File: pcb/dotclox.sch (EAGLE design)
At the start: 1 part, among them IC1 DS1307Z

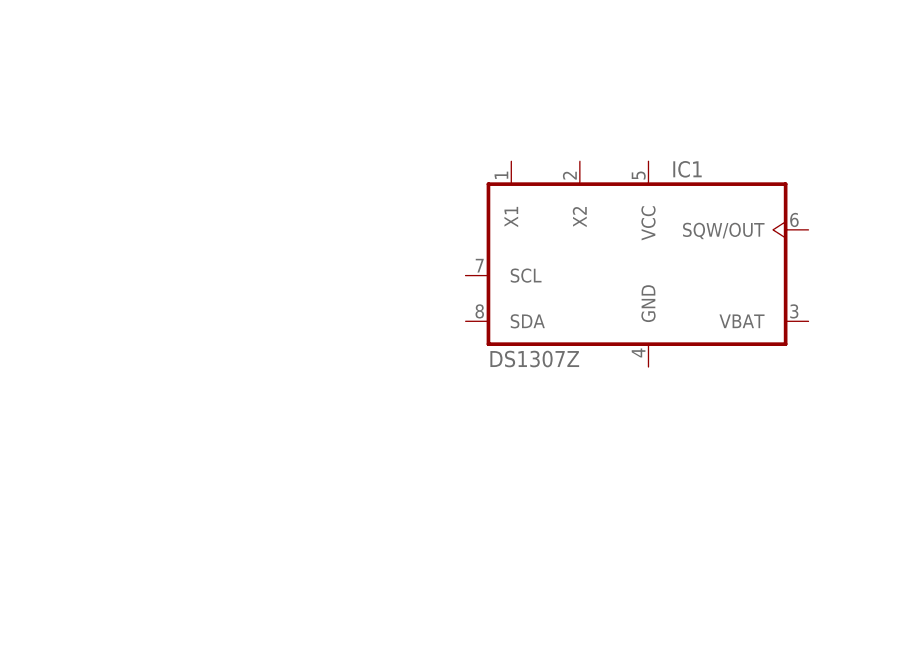
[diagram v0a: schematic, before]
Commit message: add basic parts to sch and brd
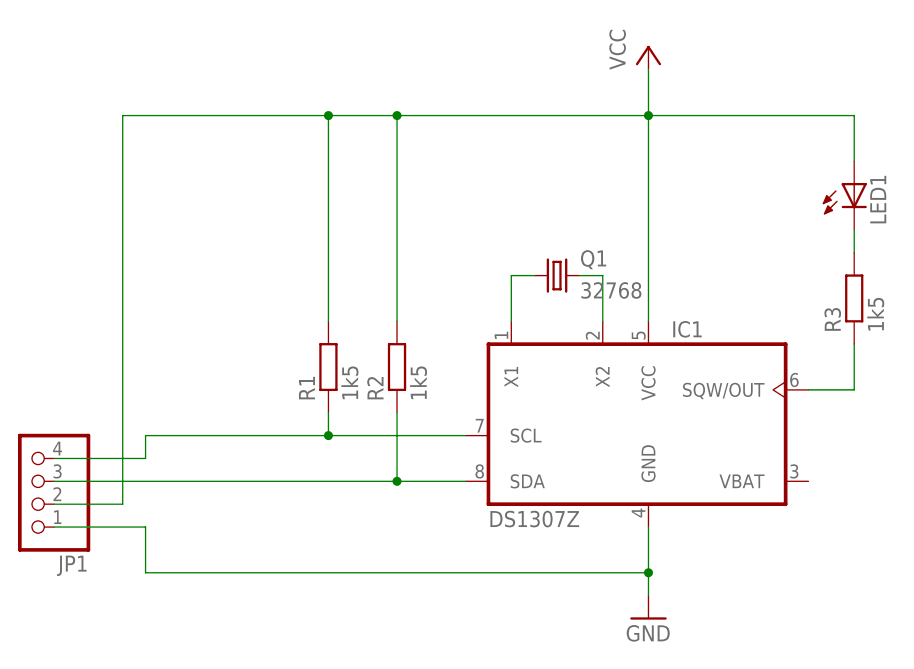
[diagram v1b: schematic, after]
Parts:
- added JP1: (no value), pinhead:PINHD-1X4
- added LED1: (no value), led:LED3MM
- added Q1: 32768, crystal:CRYSTALTC26H
- added R1, R2, R3: 1k5, rcl:R-EU_R0603
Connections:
- new net GND: IC1.GND, JP1.1
- new net N$1: IC1.X1, Q1.1
- new net N$2: IC1.X2, Q1.2
- new net N$3: IC1.SQW/OUT, R3.1
- new net N$4: LED1.C, R3.2
- new net SCL: IC1.SCL, JP1.4, R1.1
- new net SDA: IC1.SDA, JP1.3, R2.1
- new net VCC: IC1.VCC, JP1.2, LED1.A, R1.2, R2.2
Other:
- moved on the sheet: IC1
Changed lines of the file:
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@@
 <?xml version="1.0" encoding="utf-8"?>
 <!DOCTYPE eagle SYSTEM "eagle.dtd">
-<eagle version="7.2.0">
+<eagle version="7.5.0">
 <drawing>
 <settings>
@@
 <parts>
 <part name="IC1" library="n39" deviceset="DS1307" device="Z"/>
+<part name="R1" library="rcl" deviceset="R-EU_" device="R0603" value="1k5"/>
+<part name="R2" library="rcl" deviceset="R-EU_" device="R0603" value="1k5"/>
+<part name="P+1" library="supply1" deviceset="VCC" device=""/>
+<part name="GND1" library="supply1" deviceset="GND" device=""/>
+<part name="JP1" library="pinhead" deviceset="PINHD-1X4" device=""/>
+<part name="Q1" library="crystal" deviceset="CRYSTAL" device="TC26H" value="32768"/>
+<part name="R3" library="rcl" deviceset="R-EU_" device="R0603" value="1k5"/>
+<part name="LED1" library="led" deviceset="LED" device="3MM"/>
 </parts>
 <sheets>
@@
 </plain>
 <instances>
-<instance part="IC1" gate="G$1" x="71.12" y="38.1"/>
+<instance part="IC1" gate="G$1" x="71.12" y="20.32"/>
+<instance part="R1" gate="G$1" x="35.56" y="25.4" rot="R90"/>
+<instance part="R2" gate="G$1" x="43.18" y="25.4" rot="R90"/>
+<instance part="P+1" gate="VCC" x="71.12" y="60.96"/>
+<instance part="GND1" gate="1" x="71.12" y="-2.54"/>
+<instance part="JP1" gate="A" x="2.54" y="12.7" rot="R180"/>
+<instance part="Q1" gate="G$1" x="60.96" y="35.56"/>
+<instance part="R3" gate="G$1" x="93.98" y="33.02" rot="R90"/>
+<instance part="LED1" gate="G$1" x="93.98" y="45.72"/>
 </instances>
 <busses>
 </busses>
 <nets>
+<net name="SCL" class="0">
+<segment>
+<pinref part="IC1" gate="G$1" pin="SCL"/>
+<wire x1="50.8" y1="17.78" x2="35.56" y2="17.78" width="0.1524" layer="91"/>
+<pinref part="R1" gate="G$1" pin="1"/>
+<wire x1="35.56" y1="17.78" x2="15.24" y2="17.78" width="0.1524" layer="91"/>
+<wire x1="35.56" y1="20.32" x2="35.56" y2="17.78" width="0.1524" layer="91"/>
+<junction x="35.56" y="17.78"/>
+<wire x1="15.24" y1="17.78" x2="15.24" y2="15.24" width="0.1524" layer="91"/>
+<pinref part="JP1" gate="A" pin="4"/>
+<wire x1="15.24" y1="15.24" x2="5.08" y2="15.24" width="0.1524" layer="91"/>
+</segment>
+</net>
+<net name="SDA" class="0">
+<segment>
+<pinref part="IC1" gate="G$1" pin="SDA"/>
+<wire x1="50.8" y1="12.7" x2="43.18" y2="12.7" width="0.1524" layer="91"/>
+<pinref part="R2" gate="G$1" pin="1"/>
+<wire x1="43.18" y1="12.7" x2="5.08" y2="12.7" width="0.1524" layer="91"/>
+<wire x1="43.18" y1="20.32" x2="43.18" y2="12.7" width="0.1524" layer="91"/>
+<junction x="43.18" y="12.7"/>
+<pinref part="JP1" gate="A" pin="3"/>
+</segment>
+</net>
+<net name="GND" class="0">
+<segment>
+<pinref part="IC1" gate="G$1" pin="GND"/>
+<pinref part="GND1" gate="1" pin="GND"/>
+<wire x1="71.12" y1="7.62" x2="71.12" y2="2.54" width="0.1524" layer="91"/>
+<wire x1="71.12" y1="2.54" x2="71.12" y2="0" width="0.1524" layer="91"/>
+<wire x1="71.12" y1="2.54" x2="15.24" y2="2.54" width="0.1524" layer="91"/>
+<wire x1="15.24" y1="2.54" x2="15.24" y2="7.62" width="0.1524" layer="91"/>
+<pinref part="JP1" gate="A" pin="1"/>
+<wire x1="15.24" y1="7.62" x2="5.08" y2="7.62" width="0.1524" layer="91"/>
+<junction x="71.12" y="2.54"/>
+</segment>
+</net>
+<net name="VCC" class="0">
+<segment>
+<pinref part="IC1" gate="G$1" pin="VCC"/>
+<pinref part="P+1" gate="VCC" pin="VCC"/>
+<wire x1="71.12" y1="30.48" x2="71.12" y2="53.34" width="0.1524" layer="91"/>
+<pinref part="R2" gate="G$1" pin="2"/>
+<wire x1="71.12" y1="53.34" x2="71.12" y2="58.42" width="0.1524" layer="91"/>
+<wire x1="43.18" y1="30.48" x2="43.18" y2="53.34" width="0.1524" layer="91"/>
+<wire x1="43.18" y1="53.34" x2="71.12" y2="53.34" width="0.1524" layer="91"/>
+<pinref part="R1" gate="G$1" pin="2"/>
+<wire x1="35.56" y1="30.48" x2="35.56" y2="53.34" width="0.1524" layer="91"/>
+<wire x1="35.56" y1="53.34" x2="43.18" y2="53.34" width="0.1524" layer="91"/>
+<junction x="43.18" y="53.34"/>
+<junction x="71.12" y="53.34"/>
+<pinref part="JP1" gate="A" pin="2"/>
+<wire x1="5.08" y1="10.16" x2="12.7" y2="10.16" width="0.1524" layer="91"/>
+<wire x1="12.7" y1="10.16" x2="12.7" y2="53.34" width="0.1524" layer="91"/>
+<wire x1="12.7" y1="53.34" x2="35.56" y2="53.34" width="0.1524" layer="91"/>
+<junction x="35.56" y="53.34"/>
+<pinref part="LED1" gate="G$1" pin="A"/>
+<wire x1="93.98" y1="48.26" x2="93.98" y2="53.34" width="0.1524" layer="91"/>
+<wire x1="93.98" y1="53.34" x2="71.12" y2="53.34" width="0.1524" layer="91"/>
+</segment>
+</net>
+<net name="N$1" class="0">
+<segment>
+<pinref part="IC1" gate="G$1" pin="X1"/>
+<wire x1="55.88" y1="30.48" x2="55.88" y2="35.56" width="0.1524" layer="91"/>
+<pinref part="Q1" gate="G$1" pin="1"/>
+<wire x1="55.88" y1="35.56" x2="58.42" y2="35.56" width="0.1524" layer="91"/>
+</segment>
+</net>
+<net name="N$2" class="0">
+<segment>
+<pinref part="Q1" gate="G$1" pin="2"/>
+<pinref part="IC1" gate="G$1" pin="X2"/>
+<wire x1="63.5" y1="35.56" x2="66.04" y2="35.56" width="0.1524" layer="91"/>
+<wire x1="66.04" y1="35.56" x2="66.04" y2="30.48" width="0.1524" layer="91"/>
+</segment>
+</net>
+<net name="N$3" class="0">
+<segment>
+<pinref part="IC1" gate="G$1" pin="SQW/OUT"/>
+<pinref part="R3" gate="G$1" pin="1"/>
+<wire x1="88.9" y1="22.86" x2="93.98" y2="22.86" width="0.1524" layer="91"/>
+<wire x1="93.98" y1="22.86" x2="93.98" y2="27.94" width="0.1524" layer="91"/>
+</segment>
+</net>
+<net name="N$4" class="0">
+<segment>
+<pinref part="R3" gate="G$1" pin="2"/>
+<pinref part="LED1" gate="G$1" pin="C"/>
+<wire x1="93.98" y1="38.1" x2="93.98" y2="40.64" width="0.1524" layer="91"/>
+</segment>
+</net>
 </nets>
 </sheet>
